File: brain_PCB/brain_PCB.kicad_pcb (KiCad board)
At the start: 2 copper layers, 100 x 100 mm, 60 parts, among them J1 Conn_01x02, J10 Conn_01x02, J2 Conn_01x02, J3 Conn_01x02, J4 Conn_01x03, J5 Conn_01x03, J6 Conn_01x04, J7 Conn_01x14, J8 Conn_01x06, J9 Conn_01x08, SW1 SW_Push, U1 STM32H753ZITx, Y1 8 MHz, Y2 32.768 kHz

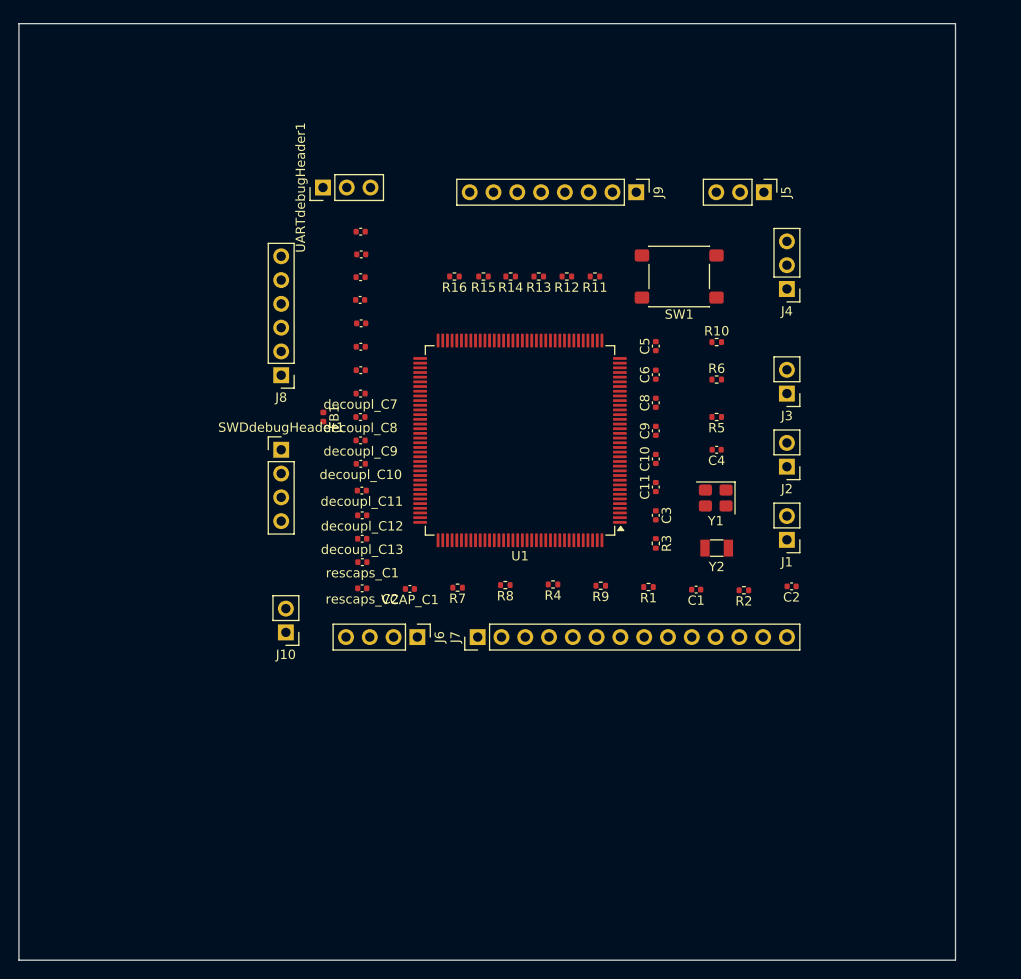
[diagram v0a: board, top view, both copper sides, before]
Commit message: brain PCB routing complete: GND pours on outer layers, stitching vias, SI fixes; electrical DRC clean
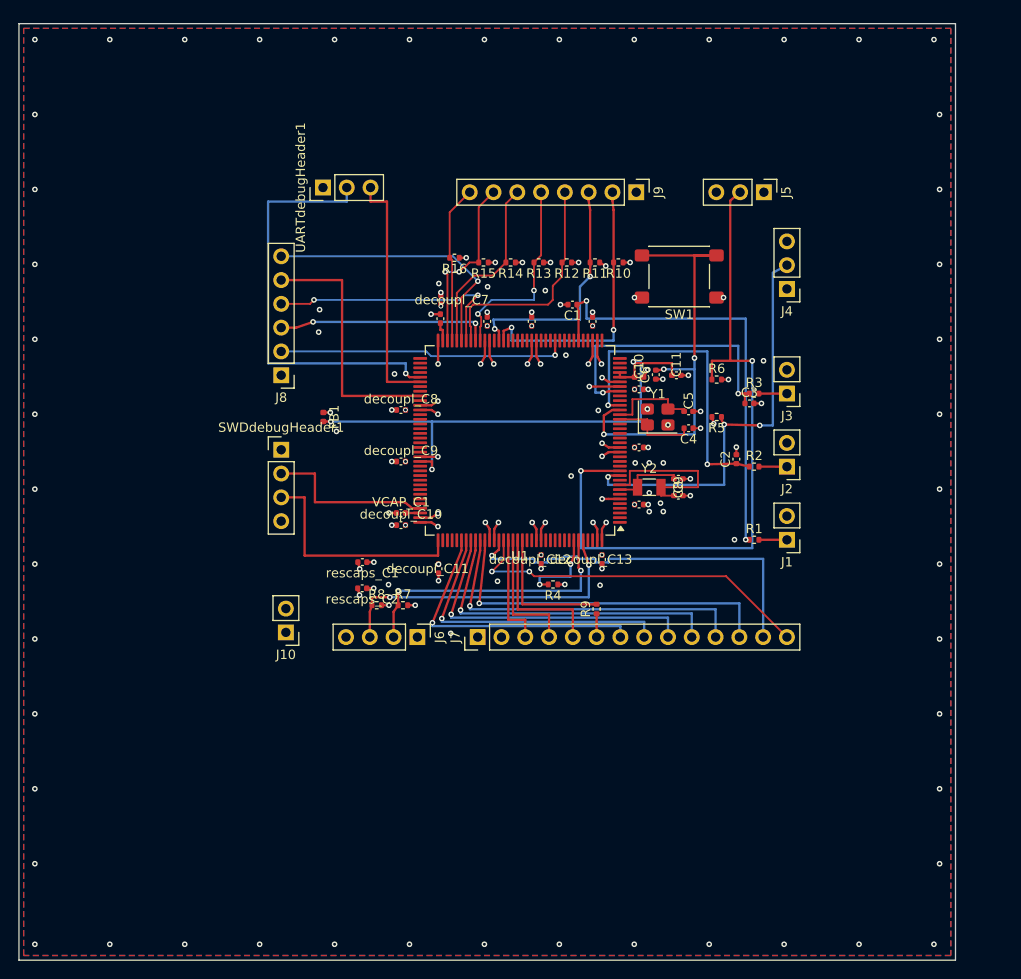
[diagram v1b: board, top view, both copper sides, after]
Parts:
- moved decoupl_C3 36.9 mm to (79.2, 63.9)
- moved decoupl_C1 36.1 mm to (79.2, 57.8)
- moved C1 33.2 mm to (72.1, 42.5)
- moved decoupl_C2 32.1 mm to (79.2, 51.5)
- moved decoupl_C13 25.7 mm to (75.2, 69.7), turned to 90 degrees
- moved decoupl_C4 24.7 mm to (74.2, 44.3), turned to -90 degrees
- moved decoupl_C12 19.7 mm to (68.8, 69.7), turned to 90 degrees
- moved R3 19.1 mm to (91.5, 52.0), turned to 0 degrees
- moved decoupl_C5 18.5 mm to (67.8, 44.3), turned to -90 degrees
- moved C3 15.6 mm to (91.0, 53.0), turned to 0 degrees
- moved C2 14.8 mm to (89.6, 59.0), turned to 90 degrees
- moved decoupl_C6 14.5 mm to (63.0, 44.3), turned to -90 degrees
- moved R8 13.9 mm to (51.2, 74.6), turned to 0 degrees
- moved R10 13.5 mm to (77.0, 38.0), turned to 180 degrees
- moved R2 13.2 mm to (91.5, 59.8), turned to 0 degrees
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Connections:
- U1 pad 124: unconnected-(U1-PG9-Pad124) -> /LCD_RST
- U1 pad 125: unconnected-(U1-PG10-Pad125) -> /LCD_CD
- U1 pad 126: unconnected-(U1-PG11-Pad126) -> /LCD_CS
- U1 pad 127: unconnected-(U1-PG12-Pad127) -> /LCD_WR
- U1 pad 96: /LCD_RST -> (no net)
- U1 pad 97: /LCD_CD -> (no net)
- U1 pad 98: /LCD_CS -> (no net)
- U1 pad 99: /LCD_WR -> (no net)
- Y1 pad 2: Net-(U1-PH1) -> GND
- Y1 pad 3: (no net) -> Net-(U1-PH1)
- Y1 pad 4: (no net) -> GND
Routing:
- net /PF2: track 0.00 -> 75.2 mm, vias 0 -> 2
- net /VDDA: track 0.00 -> 57.4 mm, vias 0 -> 3
- net /PA6: track 0.00 -> 47.8 mm, vias 0 -> 2
- net Net-(U1-NRST): track 0.00 -> 46.2 mm, vias 0 -> 3
- net GND: track 0.00 -> 45.6 mm, vias 0 -> 117
- net /PF1: track 0.00 -> 44.8 mm, vias 0 -> 3
- net /UART_TX: track 0.00 -> 44.7 mm, vias 0 -> 1
- net /LCD_D6: track 0.00 -> 41.7 mm, vias 0 -> 1
- net /LCD_D7: track 0.00 -> 38.3 mm, vias 0 -> 2
- net /LCD_D5: track 0.00 -> 38.1 mm, vias 0 -> 1
- net +3V3: track 0.00 -> 37.3 mm, vias 0 -> 36
- net /LCD_D4: track 0.00 -> 36.7 mm, vias 0 -> 1
- net /LCD_D3: track 0.00 -> 35.2 mm, vias 0 -> 1
- net /LCD_D2: track 0.00 -> 33.8 mm, vias 0 -> 1
- net /SDA: track 0.00 -> 33.6 mm, vias 0 -> 2
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- added copper zone on In2.Cu, net +3V3
- added copper zone on B.Cu, net GND
- added copper zone on F.Cu, net GND
- added copper zone on In1.Cu, net GND
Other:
- copper layers 2 -> 4

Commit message: brain PCB: resize board to 69.7x63.6mm, add M3 mounting holes, silkscreen label cleanup
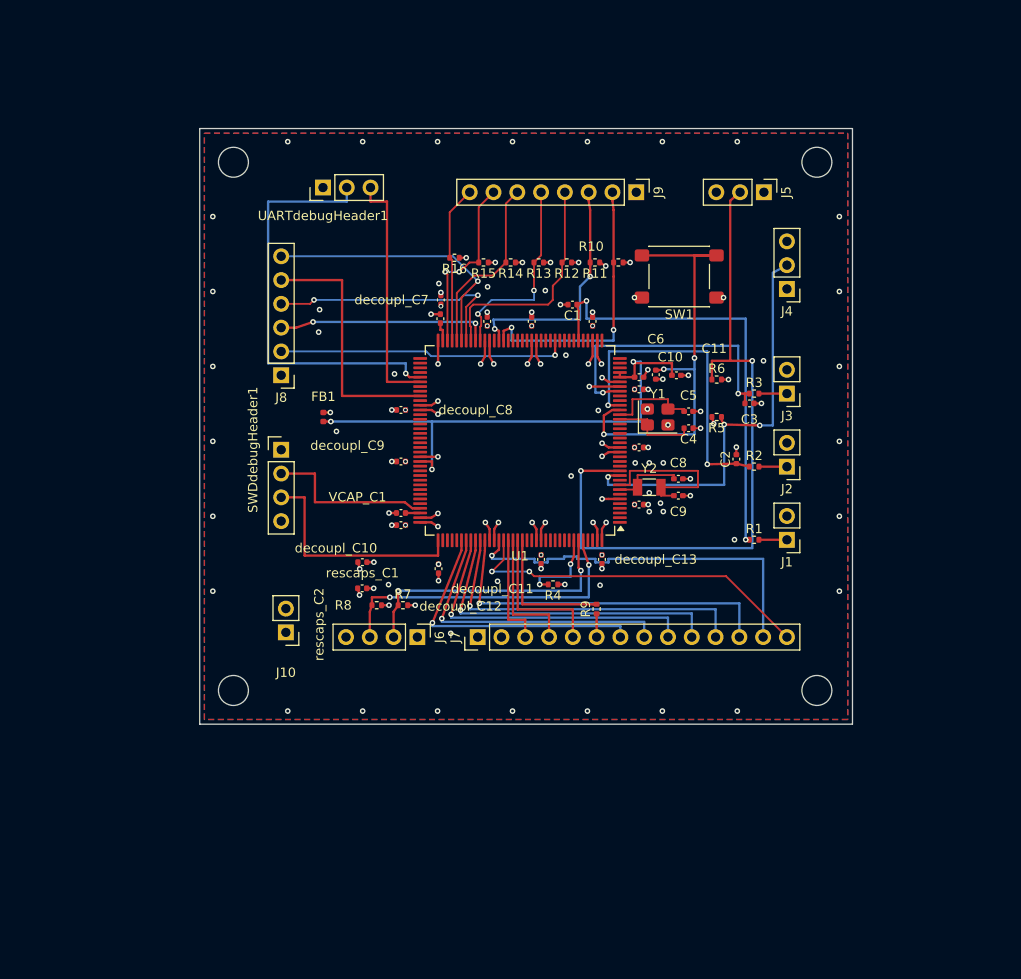
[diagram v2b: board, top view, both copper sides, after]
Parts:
- added H1: MountingHole_3.2mm_M3, MountingHole_3.2mm_M3, F.Cu at (35.9, 27.3)
- added H2: MountingHole_3.2mm_M3, MountingHole_3.2mm_M3, F.Cu at (98.2, 27.3)
- added H3: MountingHole_3.2mm_M3, MountingHole_3.2mm_M3, F.Cu at (35.9, 83.7)
- added H4: MountingHole_3.2mm_M3, MountingHole_3.2mm_M3, F.Cu at (98.2, 83.7)
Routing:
- net GND: vias 117 -> 95
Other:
- board size 100 x 100 mm -> 69.7 x 63.6 mm

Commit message: brain PCB: add connector silkscreen labels, fix decoupling cap thermal relief for SMT assembly
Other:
- board text added: "DS3231_RTC"
- board text added: "EnclTemp"
- board text added: "Hydroponic Brain Board"
- board text added: "LEVEL_IN"
- board text added: "PH_IN"
- board text added: "PWMConnector"
- board text added: "TDS_IN"
- board text added: "WaterTemp"
- board text added: "powerIn"
- board text added: "pumpConnector"
- board text added: "screenConnector"
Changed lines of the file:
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@@
 		(tags "Through hole pin header THT 1x04 2.54mm single row")
 		(property "Reference" "SWDdebugHeader1"
-			(at -3.01325 0 90)
+			(at -3 2.5 90)
 			(layer "F.SilkS")
 			(effects
@@
 			(at 0 7.46 90)
 			(layer "F.Fab")
+			(hide yes)
 			(effects
 				(font
@@
 		(tags "Through hole pin header THT 1x03 2.54mm single row")
 		(property "Reference" "UARTdebugHeader1"
-			(at -3.01325 0 0)
+			(at 3 2.04 0)
 			(layer "F.SilkS")
 			(effects
@@
 			(net "GND")
 			(pintype "passive")
-			(zone_connect 2)
 		)
 		(pad "2" smd roundrect
@@
 			(net "GND")
 			(pintype "passive")
-			(zone_connect 2)
 		)
 		(pad "2" smd roundrect
@@
 		(layer "Edge.Cuts")
 	)
+	(gr_text "EnclTemp"
+		(at 90 28 0)
+		(layer "F.SilkS")
+		(effects
+			(font
+				(size 1 1)
+				(thickness 0.15)
+			)
+		)
+	)
+	(gr_text "DS3231_RTC"
+		(at 52 81 0)
+		(layer "F.SilkS")
+		(effects
+			(font
+				(size 1.2 1.2)
+				(thickness 0.15)
+			)
+		)
+	)
+	(gr_text "pumpConnector"
+		(at 69.5 27.5 0)
+		(layer "F.SilkS")
+		(effects
+			(font
+				(size 1.2 1.2)
+				(thickness 0.15)
+			)
+		)
+	)
+	(gr_text "screenConnector"
+		(at 78.5 81 0)
+		(layer "F.SilkS")
+		(effects
+			(font
+				(size 1.2 1.2)
+				(thickness 0.15)
+			)
+		)
+	)
+	(gr_text "PWMConnector"
+		(at 38 44.5 90)
+		(layer "F.SilkS")
+		(effects
+			(font
+				(size 1.2 1.2)
+				(thickness 0.15)
+			)
+		)
+	)
+	(gr_text "powerIn"
+		(at 38 77 90)
+		(layer "F.SilkS")
+		(effects
+			(font
+				(size 1.2 1.2)
+				(thickness 0.15)
+			)
+		)
+	)
+	(gr_text "LEVEL_IN"
+		(at 98 50.5 90)
+		(layer "F.SilkS")
+		(effects
+			(font
+				(size 1.2 1.2)
+				(thickness 0.15)
+			)
+		)
+	)
+	(gr_text "PH_IN"
+		(at 98 58.537 90)
+		(layer "F.SilkS")
+		(effects
+			(font
+				(size 1.2 1.2)
+				(thickness 0.15)
+			)
+		)
+	)
+	(gr_text "TDS_IN"
+		(at 98 66.5 90)
+		(layer "F.SilkS")
+		(effects
+			(font
+				(size 1.2 1.2)
+				(thickness 0.15)
+			)
+		)
+	)
+	(gr_text "WaterTemp"
+		(at 98 38.5 270)
+		(layer "F.SilkS")
+		(effects
+			(font
+				(size 1.2 1.2)
+				(thickness 0.15)
+			)
+		)
+	)
+	(gr_text "Hydroponic Brain Board"
+		(at 53.5 84.5 0)
+		(layer "F.SilkS")
+		(effects
+			(font
+				(size 1.5 1.5)
+				(thickness 0.3)
+				(bold yes)
+			)
+			(justify left bottom)
+		)
+	)
 	(segment

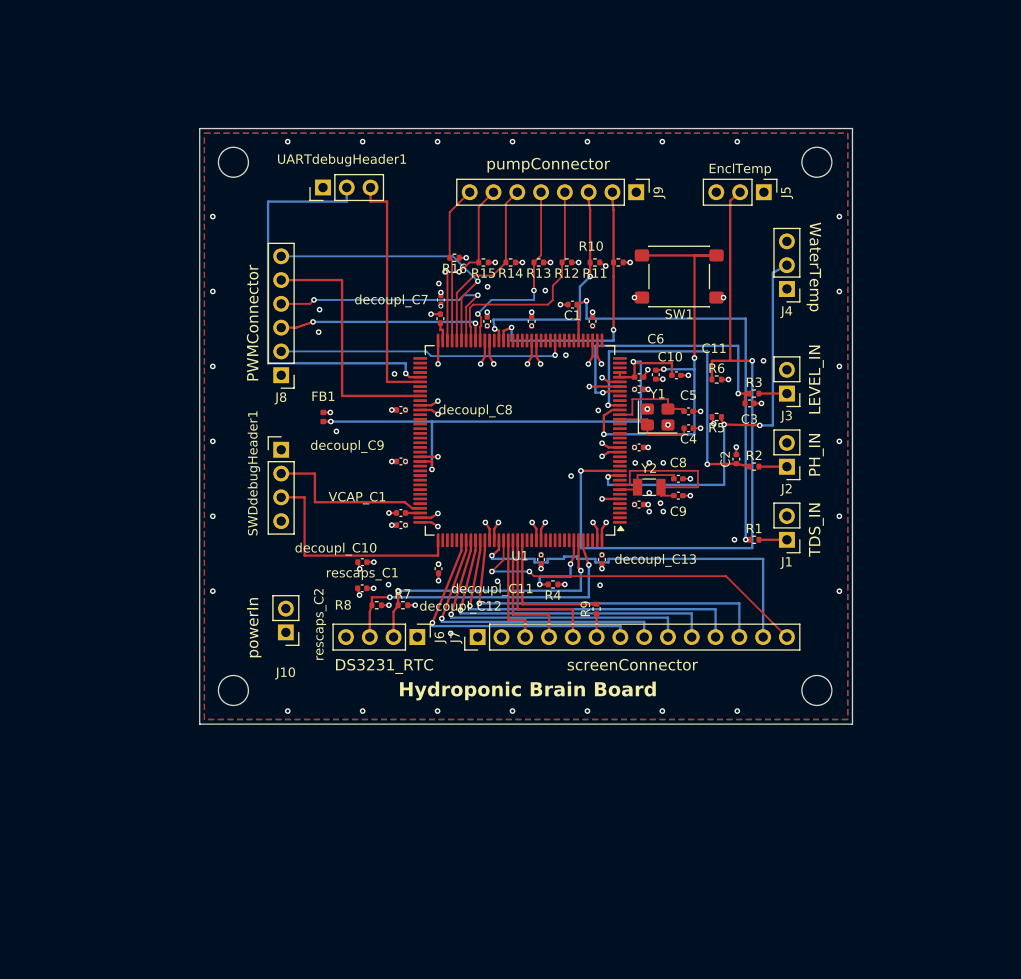
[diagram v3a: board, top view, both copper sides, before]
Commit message: all boards routed: light rev B (SOT-23 switches, protected input), pump rev B (CSD18540 MOSFETs), power rev A1 (parts selected), brain Micro-Fit connectors + display on edge; whitelist gitignore
Light, power and pump pass DRC and ERC clean. Brain routed with 0 unconnected; remaining warnings are dangling vias, thin silk text and missing no-connect flags. All cable connectors standardized to Molex Micro-Fit 3.0. Repo now tracks only the KiCad project files, design rules, local libraries and brain 3D models.
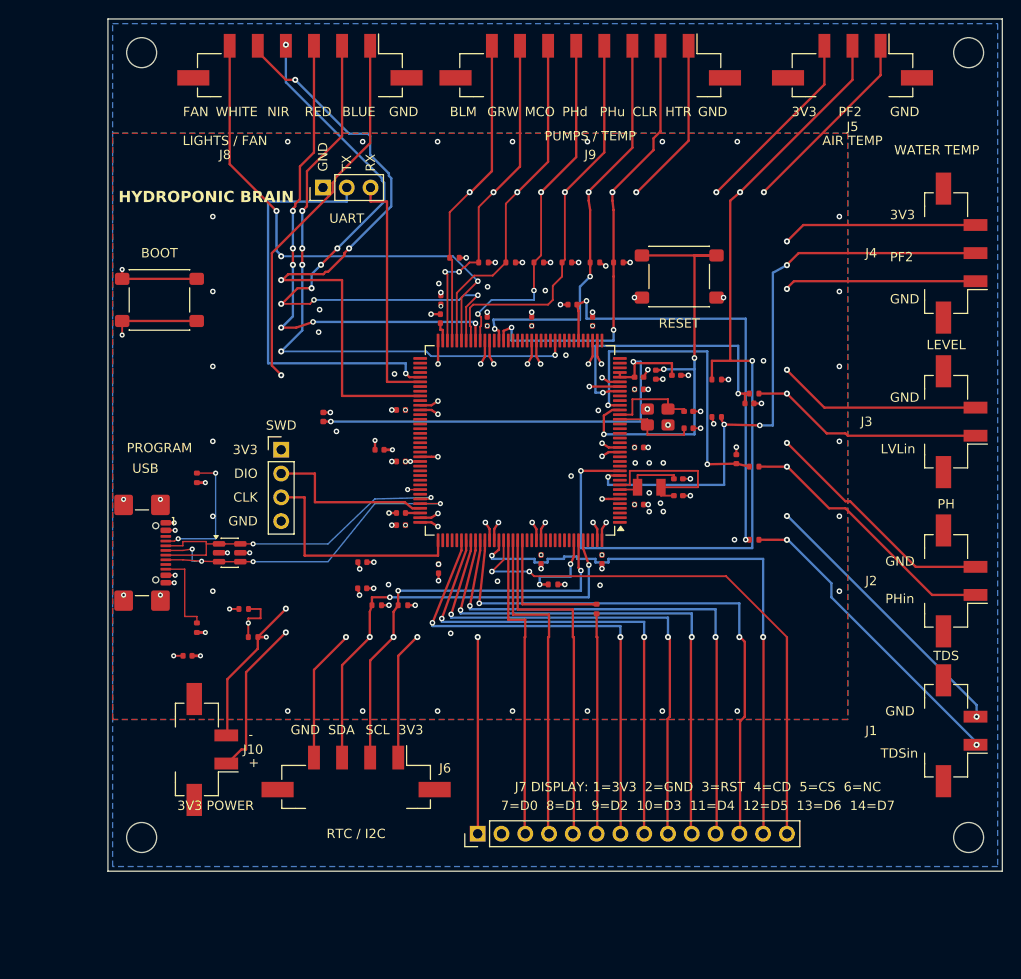
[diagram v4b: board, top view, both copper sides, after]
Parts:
- added C12: 100nF, Capacitor_SMD:C_0402_1005Metric, F.Cu at (31.0, 80.0)
- added C13: 1uF, Capacitor_SMD:C_0402_1005Metric, F.Cu at (51.5, 58.0)
- added J11: USB-C PROGRAM, Connector_USB:USB_C_Receptacle_GCT_USB4110, F.Cu at (25.0, 69.0)
- added R17: 5.1k, Resistor_SMD:R_0402_1005Metric, F.Cu at (32.0, 61.0)
- added R18: 5.1k, Resistor_SMD:R_0402_1005Metric, F.Cu at (32.0, 77.0)
- added R19: 33k, Resistor_SMD:R_0402_1005Metric, F.Cu at (37.0, 75.0)
- added R20: 82k, Resistor_SMD:R_0402_1005Metric, F.Cu at (38.0, 78.0)
- added SW2: BOOT, Button_Switch_SMD:SW_SPST_PTS645Sx43SMTR92, F.Cu at (28.0, 42.0)
- added U2: USBLC6-2SC6, Package_TO_SOT_SMD:SOT-23-6, F.Cu at (35.5, 69.0)
- J1, J10, J2, J3: footprint Connector_PinHeader_2.54mm:PinHeader_1x02_P2.54mm_Vertical -> Connector_Molex:Molex_Micro-Fit_3.0_43650-0224_1x02-1MP_P3.00mm_Vertical
- J4, J5: footprint Connector_PinHeader_2.54mm:PinHeader_1x03_P2.54mm_Vertical -> Connector_Molex:Molex_Micro-Fit_3.0_43650-0324_1x03-1MP_P3.00mm_Vertical
- J6: footprint Connector_PinHeader_2.54mm:PinHeader_1x04_P2.54mm_Vertical -> Connector_Molex:Molex_Micro-Fit_3.0_43650-0424_1x04-1MP_P3.00mm_Vertical
- J8: footprint Connector_PinHeader_2.54mm:PinHeader_1x06_P2.54mm_Vertical -> Connector_Molex:Molex_Micro-Fit_3.0_43650-0624_1x06-1MP_P3.00mm_Vertical
- J9: footprint Connector_PinHeader_2.54mm:PinHeader_1x08_P2.54mm_Vertical -> Connector_Molex:Molex_Micro-Fit_3.0_43650-0824_1x08-1MP_P3.00mm_Vertical
- moved J8 32.1 mm to (43.0, 18.0)
- moved J1 26.5 mm to (112.0, 88.0), turned to 90 degrees
- moved H4 22.6 mm to (114.4, 99.4)
- moved J7 21.0 mm to (62.0, 99.0)
- moved J2 20.9 mm to (112.0, 72.0), turned to 90 degrees
- moved H2 20.0 mm to (114.4, 15.6)
- moved H3 18.5 mm to (26.1, 99.4)
- moved J4 17.4 mm to (112.0, 37.0), turned to 90 degrees
- moved J6 17.3 mm to (49.0, 94.0), turned to 180 degrees
- moved J3 17.3 mm to (112.0, 55.0), turned to 90 degrees
- moved J10 15.7 mm to (32.0, 90.0), turned to 90 degrees
- moved J5 15.7 mm to (102.0, 18.0), turned to 180 degrees
- moved H1 15.3 mm to (26.1, 15.6)
- moved J9 13.4 mm to (74.0, 18.0), turned to 180 degrees
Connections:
- net Net-(U1-BOOT0) renamed /BOOT0
- U1 pad 101: unconnected-(U1-PA9-Pad101) -> /USB_VBUS_SENSE
- U1 pad 103: unconnected-(U1-PA11-Pad103) -> /USB_DM
- U1 pad 104: unconnected-(U1-PA12-Pad104) -> /USB_DP
- U1 pad 95: /VDDA -> +3V3
- U1 pad 96: (no net) -> unconnected-(U1-PC6-Pad96)
- U1 pad 97: (no net) -> unconnected-(U1-PC7-Pad97)
- U1 pad 98: (no net) -> unconnected-(U1-PC8-Pad98)
- U1 pad 99: (no net) -> unconnected-(U1-PC9-Pad99)
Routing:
- net GND: track 45.6 -> 264.1 mm, vias 95 -> 116
- net /BOOT0: track 9.01 -> 120.7 mm, vias 2 -> 3
- net +3V3: track 37.3 -> 141.9 mm, vias 36 -> 44
- net /USB_VBUS: track 0.00 -> 88.9 mm, vias 0 -> 5
- net /WHITE_PWM: track 27.2 -> 67.6 mm, vias 0 -> 3
- net /USB_VBUS_SENSE: track 0.00 -> 39.7 mm, vias 0 -> 2
- net /USB_DP: track 0.00 -> 39.6 mm, vias 0 -> 4
- net /NIR_PWM: track 26.7 -> 64.5 mm, vias 2 -> 7
- net /USB_DM: track 0.00 -> 37.7 mm, vias 0 -> 2
- net /BLUE_PWM: track 31.0 -> 66.6 mm, vias 1 -> 5
- net /RED_PWM: track 22.8 -> 54.7 mm, vias 2 -> 6
- net /TDS_IN: track 2.99 -> 33.6 mm, vias 0 -> 2
- net /PH_IN: track 2.99 -> 29.1 mm, vias 0 -> 1
- net /FAN_PWM: track 29.2 -> 54.1 mm, vias 1 -> 3
- net /LEVEL_IN: track 2.99 -> 25.2 mm, vias 0 -> 1
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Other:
- board size 69.7 x 63.6 mm -> 95.5 x 91 mm
- board text added: "+"
- board text added: "-"
- board text added: "3V3"
- board text added: "3V3 POWER"
- board text added: "7=D0 8=D1 9=D2 10=D3 11=D4 12=D5 13=D6 14=D7"
- board text added: "AIR TEMP"
- board text added: "BLM"
- board text added: "BLUE"
- board text added: "BOOT"
- board text added: "CLK"
- board text added: "CLR"
- board text added: "DIO"
- board text added: "FAN"
- board text added: "GND"
- board text added: "GRW"
- board text added: "HTR"
- board text added: "HYDROPONIC BRAIN"
- board text added: "J7 DISPLAY: 1=3V3 2=GND 3=RST 4=CD 5=CS 6=NC"
- board text added: "LEVEL"
- board text added: "LIGHTS / FAN"
- board text added: "LVLin"
- board text added: "MCO"
- board text added: "NIR"
- board text added: "PF2"
- board text added: "PH"
- board text added: "PHd"
- board text added: "PHin"
- board text added: "PHu"
- board text added: "PROGRAM"
- board text added: "PUMPS / TEMP"
- board text added: "RED"
- board text added: "RESET"
- board text added: "RTC / I2C"
- board text added: "RX"
- board text added: "SCL"
- board text added: "SDA"
- board text added: "SWD"
- board text added: "TDS"
- board text added: "TDSin"
- board text added: "TX"
- board text added: "UART"
- board text added: "USB"
- board text added: "WATER TEMP"
- board text added: "WHITE"
- board text removed: "DS3231_RTC"
- board text removed: "EnclTemp"
- board text removed: "Hydroponic Brain Board"
- board text removed: "LEVEL_IN"
- board text removed: "PH_IN"
- board text removed: "PWMConnector"
- board text removed: "TDS_IN"
- board text removed: "WaterTemp"
- board text removed: "powerIn"
- board text removed: "pumpConnector"
- board text removed: "screenConnector"
